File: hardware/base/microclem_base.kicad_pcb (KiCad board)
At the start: 2 copper layers, 160 x 100 mm, 59 parts, among them U1 74AHC02, U12 74AHC14, U13 74AHC08, U14 74AHC32, U15 74HC590, U16 74AC163, U17 74AC163, U18 74AHCT245, U19 74HC590, U20 74HC590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

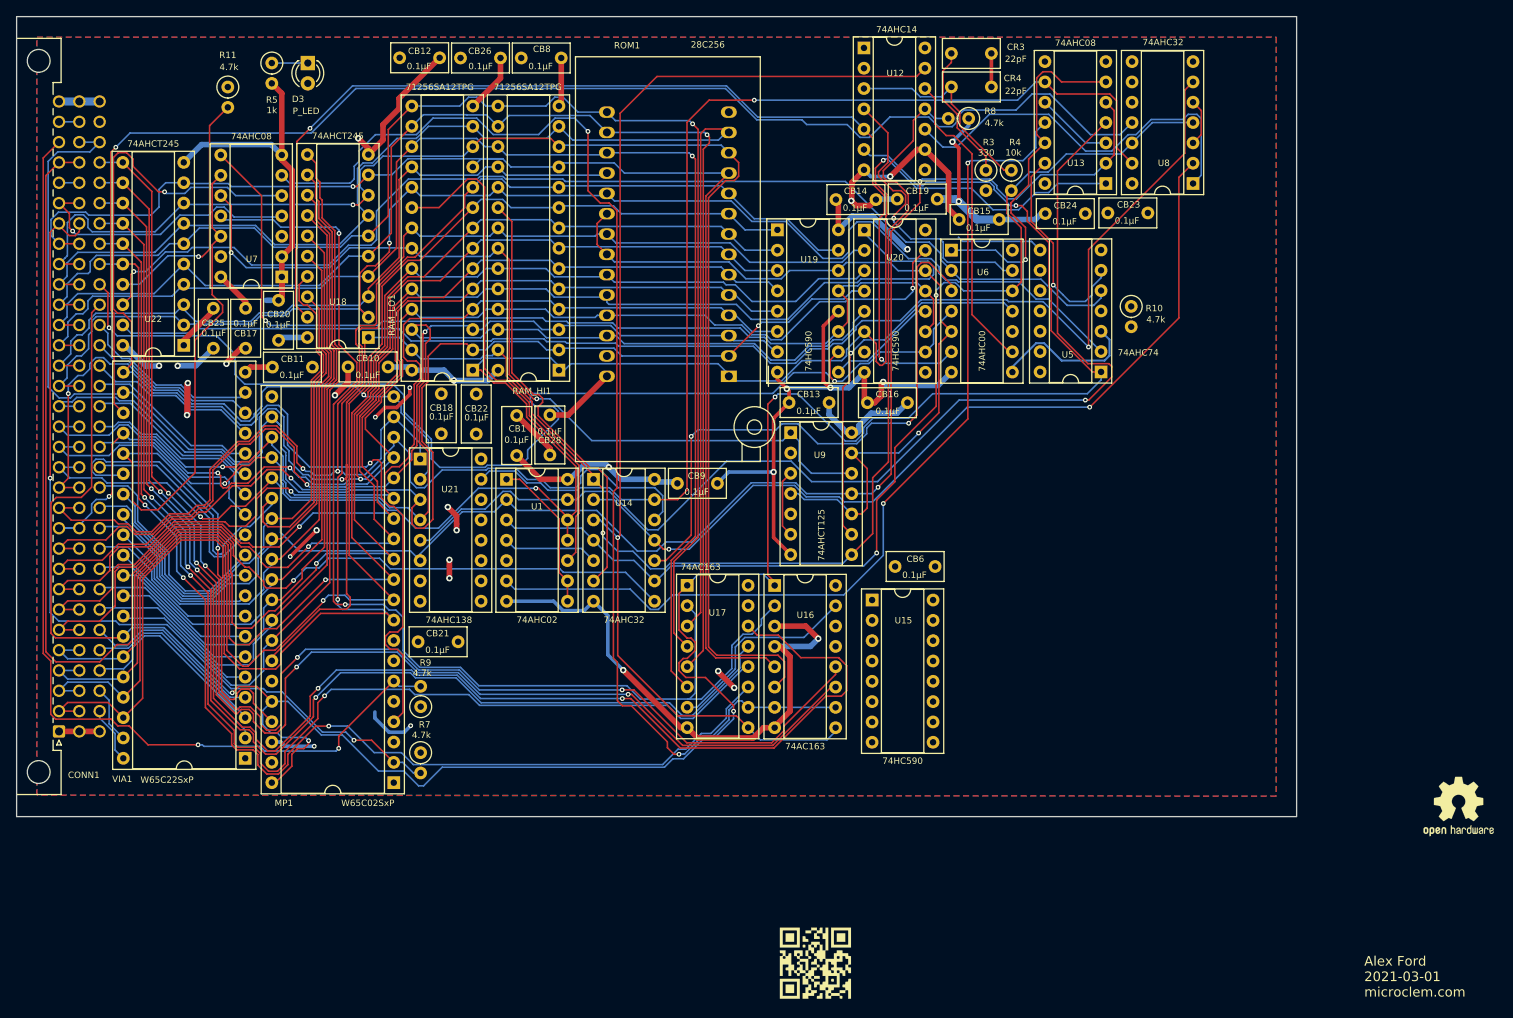
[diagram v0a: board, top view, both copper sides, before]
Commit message: base: first pass at re-routing
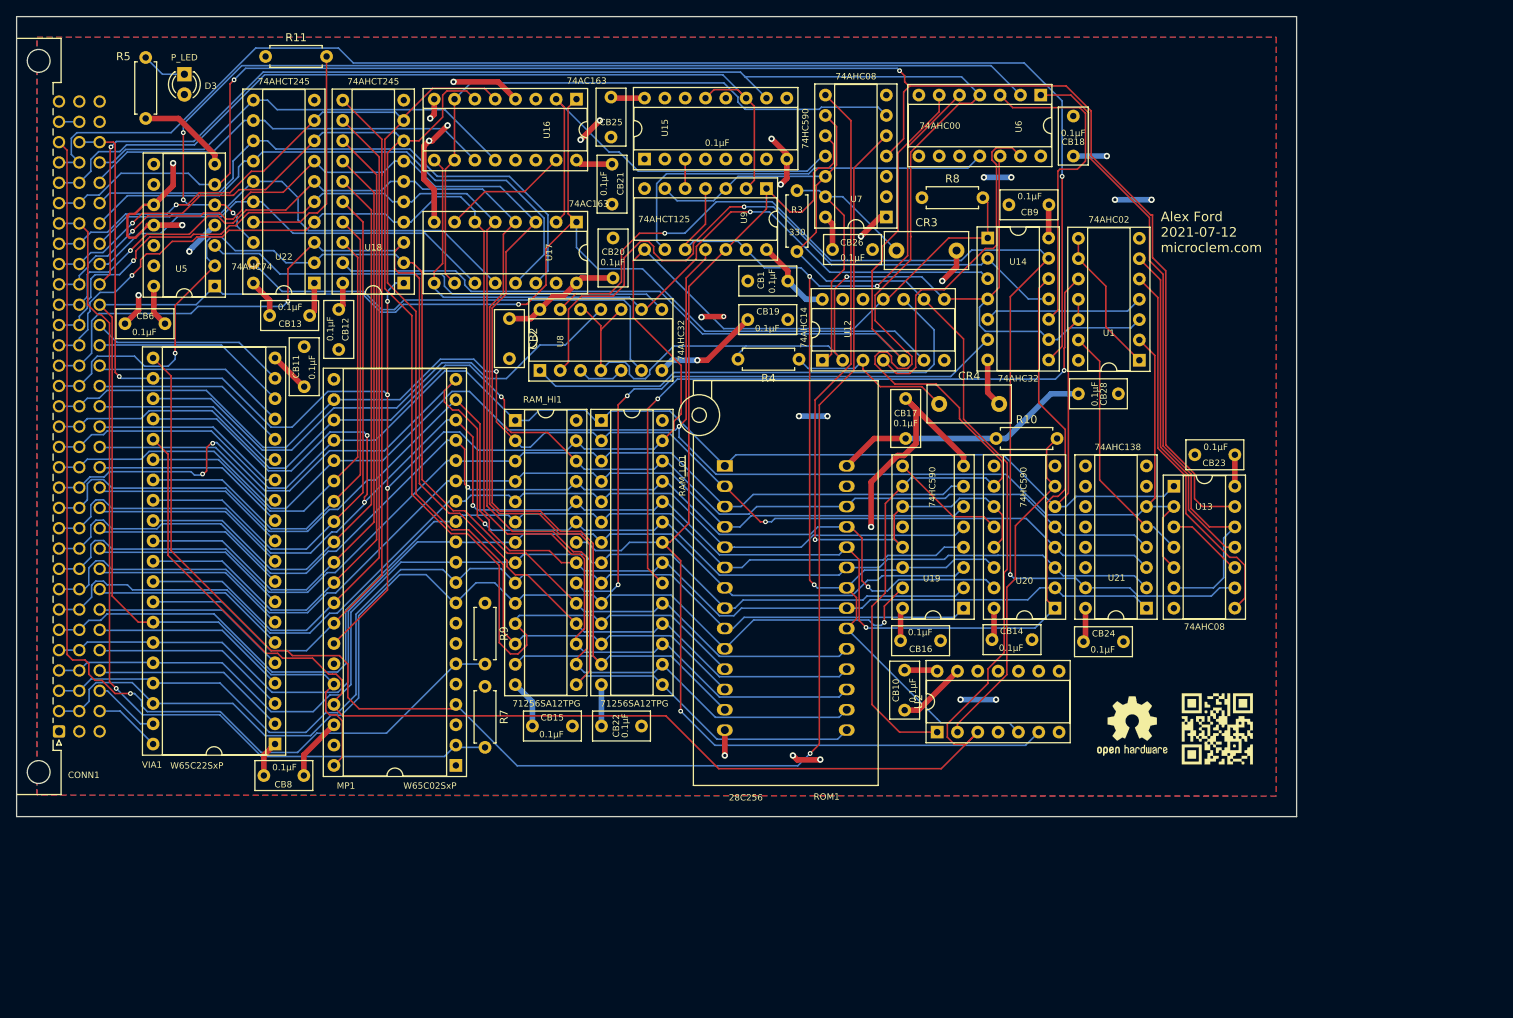
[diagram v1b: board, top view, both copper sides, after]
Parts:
- added CB2: 0.1μF, Capacitor_THT:C_Rect_L7.0mm_W3.5mm_P5.00mm, F.Cu at (84.2, 59.9)
- added U2: 74AHC74, Package_DIP:DIP-14_W7.62mm_Socket, F.Cu at (137.7, 111.6)
- CR3, CR4: footprint Capacitor_THT:C_Rect_L7.0mm_W3.5mm_P5.00mm -> Capacitor_THT:C_Rect_L10.3mm_W4.5mm_P7.50mm_MKS4
- R10, R11, R3, R4, R5, R7, R8, R9: footprint Resistor_THT:R_Axial_DIN0207_L6.3mm_D2.5mm_P2.54mm_Vertical -> Resistor_THT:R_Axial_DIN0207_L6.3mm_D2.5mm_P7.62mm_Horizontal
- moved U5 111.3 mm to (47.4, 55.9)
- moved CB6 100.9 mm to (41.1, 60.6)
- moved LOGO1 98.0 mm to (170.7, 35.1)
- moved CB8 93.7 mm to (58.5, 117.1), turned to 180 degrees
- moved U21 92.7 mm to (163.8, 96.1), turned to 180 degrees
- moved U8 84.9 mm to (88.0, 66.4), turned to 90 degrees
- moved CB18 84.4 mm to (154.7, 39.6), turned to 90 degrees
- moved CB17 84.1 mm to (133.7, 74.9), turned to 90 degrees
- moved CB15 82.8 mm to (92.1, 110.9)
- moved U1 80.5 mm to (162.9, 65.2), turned to 180 degrees
- moved U7 75.9 mm to (131.3, 47.2)
- moved CB10 74.9 mm to (133.6, 103.9), turned to 270 degrees
- moved CB13 70.8 mm to (54.2, 59.6), turned to 0 degrees
- moved CB28 66.1 mm to (155.3, 69.3), turned to 0 degrees
- moved U16 65.6 mm to (92.6, 32.5), turned to 270 degrees
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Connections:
- R4 pad 2: ~PHI_2~ -> ~BOARD_CLK~
- U1 pad 3: ~PHI_2~ -> ~BOARD_CLK~
- U12 pad 12: BUS_STATUS_W -> (no net)
- U12 pad 13: ~BUS_STATUS_W~ -> (no net)
- U12 pad 2: ~PHI_2~ -> ~BOARD_CLK~
- U12 pad 8: Net-(U12-Pad8) -> ~BOARD_CLK~
- U12 pad 9: GND -> BOARD_CLK
- U14 pad 4: ~PHI_2~ -> ~BOARD_CLK~
- U14 pad 9: ~PHI_2~ -> ~BOARD_CLK~
- U5 pad 10: +5V -> GND
- U5 pad 11: BOARD_CLK -> GND
- U5 pad 12: Net-(R10-Pad2) -> GND
- U5 pad 13: ~RST~ -> GND
- U5 pad 8: CPY -> Net-(U5-Pad8)
- U5 pad 9: ~CPY~ -> Net-(U5-Pad9)
- U6 pad 10: BOARD_CLK -> GND
- U6 pad 12: ~PHI_2~ -> ~BOARD_CLK~
- U6 pad 8: Net-(U5-Pad3) -> Net-(U6-Pad8)
- U6 pad 9: BUS_STATUS_W -> GND
- U8 pad 10: GND -> ~BOARD_CLK~
- U8 pad 12: ~PHI_2~ -> ~BOARD_CLK~
- U8 pad 4: ~PHI_2~ -> ~BOARD_CLK~
- U8 pad 8: Net-(U8-Pad8) -> Net-(U5-Pad3)
- U8 pad 9: GND -> ~BUS_STATUS_W~
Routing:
- net ~BUS_ACTIVE~: track 61.7 -> 215.7 mm
- net BOARD_CLK: track 112.7 -> 259.8 mm, vias 1 -> 0
- net GND: track 313.4 -> 169.0 mm, vias 24 -> 20
- net ~PHI_2~: track 137.3 -> 0.00 mm, vias 2 -> 0
- net ~BOARD_CLK~: track 0.00 -> 124.1 mm, vias 0 -> 1
- net /bd0: track 171.9 -> 55.8 mm, vias 4 -> 0
- net /bd1: track 167.6 -> 52.4 mm, vias 4 -> 0
- net ~RST~: track 145.6 -> 260.7 mm, vias 2 -> 1
- net Net-(U1-Pad13): track 140.5 -> 31.4 mm, vias 1 -> 0
- net PHI_2: track 2.54 -> 111.7 mm
- net ~BUS_STATUS_R~: track 167.9 -> 58.9 mm, vias 1 -> 0
- net /bd2: track 182.0 -> 73.5 mm, vias 4 -> 0
- net ~S_IO~: track 173.1 -> 67.6 mm, vias 1 -> 0
- net ~MP_RST~: track 318.4 -> 219.7 mm, vias 5 -> 1
- net BCC: track 146.2 -> 54.4 mm, vias 2 -> 0
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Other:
- board text added: "Alex Ford 2021-07-12 microclem.com"
- board text removed: "Alex Ford 2021-03-01 microclem.com"

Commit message: slightly increase ground plane coverage
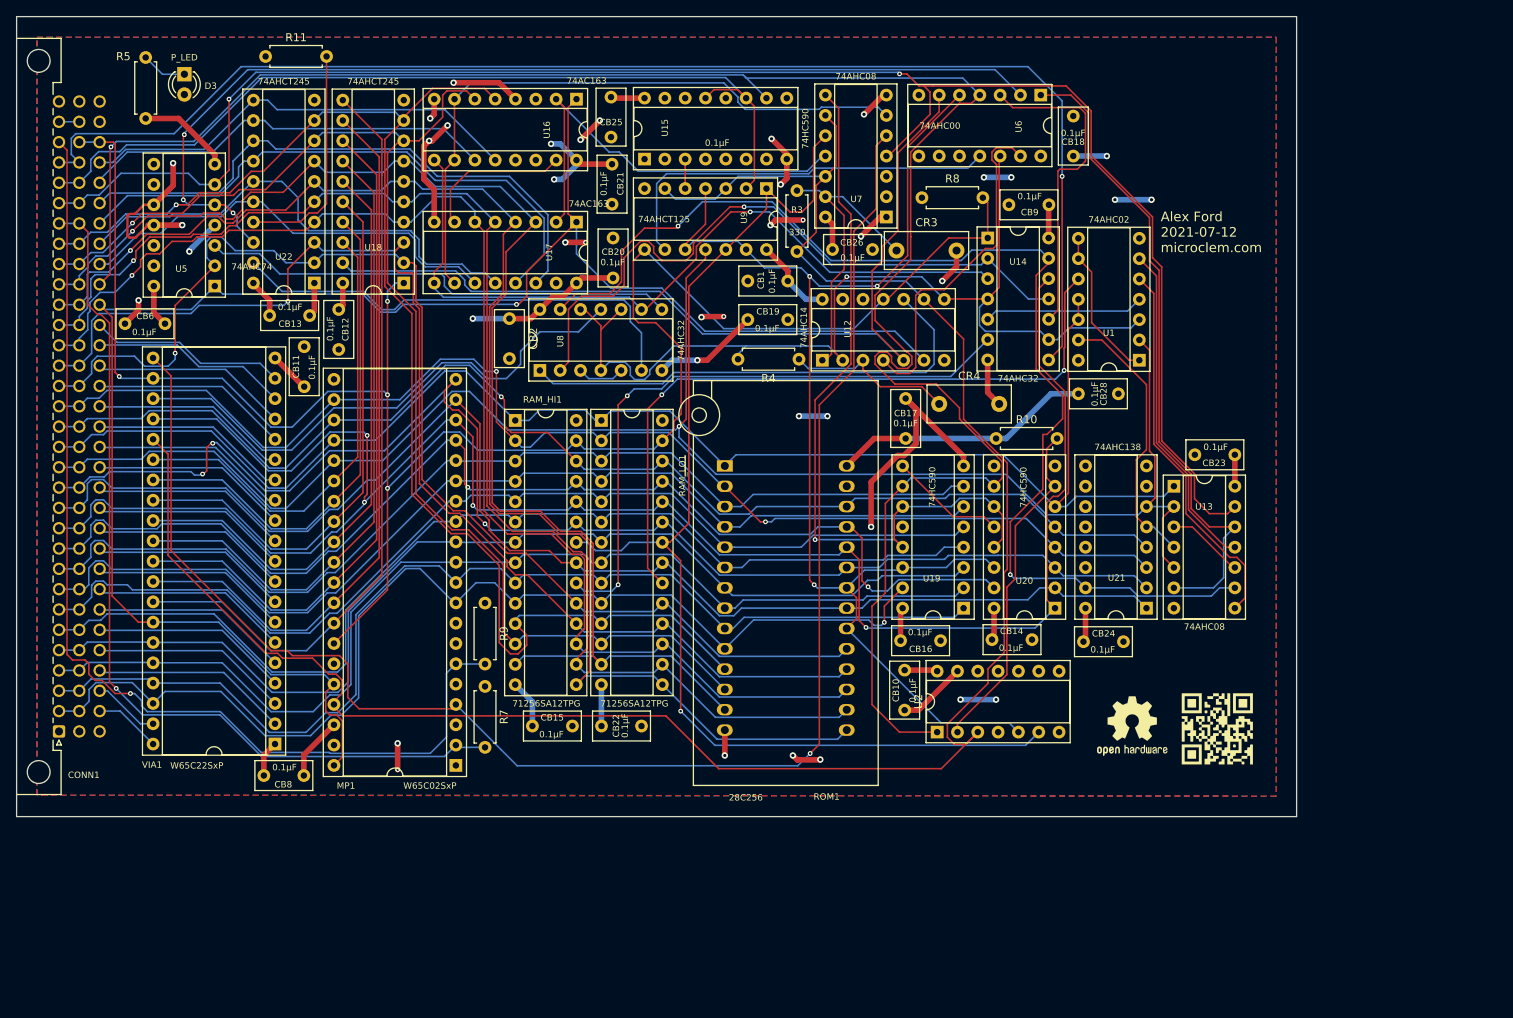
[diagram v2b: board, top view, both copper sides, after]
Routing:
- net GND: track 169.0 -> 182.3 mm, vias 20 -> 27
- net +5V: track 147.7 -> 160.4 mm, vias 10 -> 13
- net ~NMI~: track 127.5 -> 132.3 mm
- net Net-(U16-Pad15): track 15.9 -> 19.0 mm
- net /c000-c3ff: track 144.0 -> 147.1 mm
- net Net-(U1-Pad13): track 31.4 -> 34.1 mm
- net ~S_BUS~: track 170.3 -> 168.4 mm
- net /a0: track 137.4 -> 139.3 mm
- net CPY: track 149.0 -> 147.4 mm
- net /bd4: track 59.6 -> 60.9 mm
- net R~W~: track 245.8 -> 247.0 mm
- net /bd5: track 54.7 -> 56.0 mm
- net BUS_ACTIVE: track 130.3 -> 129.1 mm
- net ~S_IO~: track 67.6 -> 68.5 mm
- net Net-(U1-Pad1): track 18.4 -> 19.1 mm

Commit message: base: route optimization, label positioning
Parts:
- moved LOGO3 11.6 mm to (173.4, 113.4)
- moved LOGO2 10.9 mm to (161.9, 112.4)
- moved LOGO1 1.98 mm to (172.1, 33.7)
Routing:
- net GND: track 182.3 -> 142.7 mm, vias 27 -> 40
- net /a0: track 139.3 -> 128.3 mm
- net ~RST~: track 260.4 -> 250.8 mm
- net RDY: track 113.7 -> 123.0 mm
- net /a1: track 138.4 -> 130.2 mm
- net +5V: track 160.4 -> 167.2 mm, vias 13 -> 21
- net ~CPY~: track 159.8 -> 166.4 mm
- net /a2: track 134.5 -> 130.9 mm
- net ~BUS_ACTIVE~: track 215.7 -> 212.3 mm
- net BOARD_CLK: track 259.6 -> 256.5 mm
- net /c000-c3ff: track 147.1 -> 144.4 mm
- net /a14: track 187.6 -> 189.8 mm
- net ~IRQ~: track 200.7 -> 198.7 mm
- net /d3: track 176.3 -> 174.4 mm
- net /bd4: track 60.9 -> 59.3 mm
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
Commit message: base: big logo
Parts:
- LOGO1: footprint graphics:microclem_logo_mask -> graphics:microclem_logo_mask_large
- moved CB24 3.66 mm to (159.6, 100.3)
- moved LOGO1 1.86 mm to (170.5, 34.7)
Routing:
- net +5V: track 167.2 -> 168.5 mm
